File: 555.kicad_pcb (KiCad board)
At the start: 2 copper layers, 120 x 35 mm, 62 parts, among them J2 Screw_Terminal_01x02, P1 USB_C_Plug, SW1 SW_Push, SW2 SW_Push, SW3 SW_Push, SW4 SW_Push, SW5 SW_Push, SW6 SW_Push, SW7 SW_Push, SW8 SW_Push, U1 NE555P

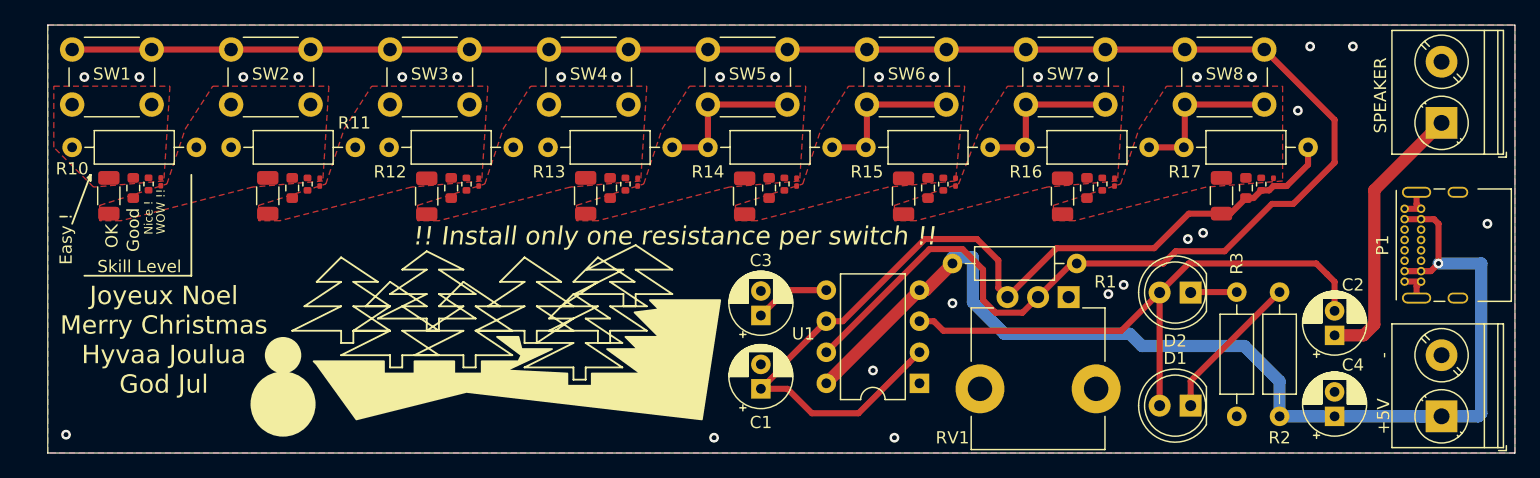
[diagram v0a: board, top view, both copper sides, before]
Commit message: Simpler, remove the 10k resistor, move the potentiometer to full to play
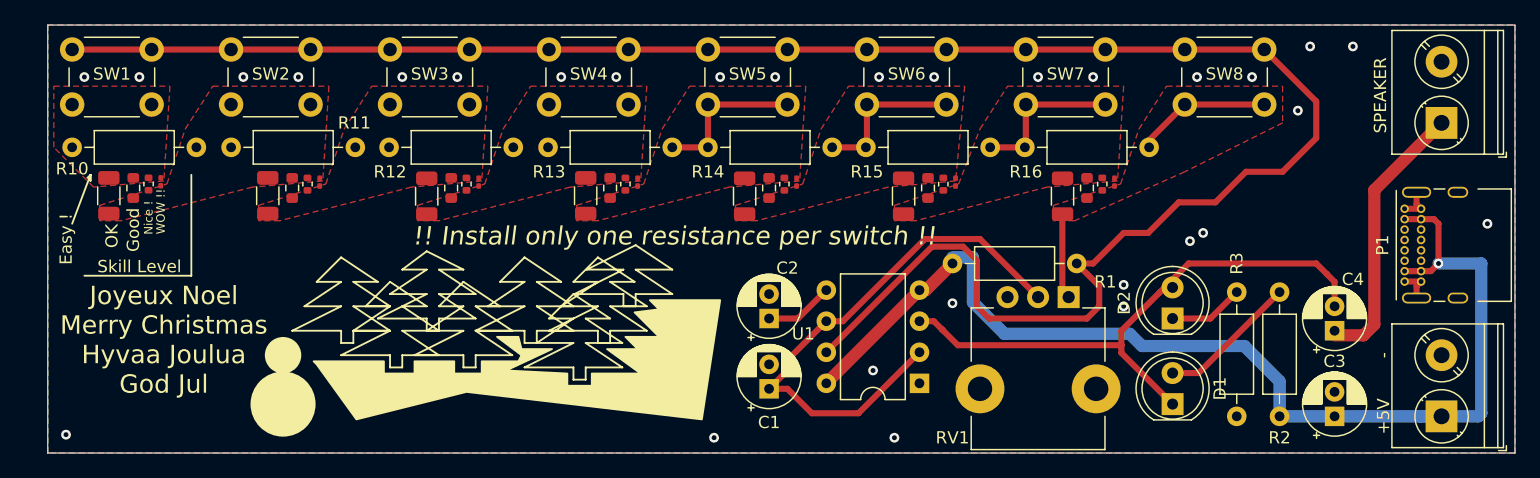
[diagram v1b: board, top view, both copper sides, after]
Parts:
- removed R17: 10k, Resistor_THT:R_Axial_DIN0207_L6.3mm_D2.5mm_P10.16mm_Horizontal
- removed R27: 10k, Resistor_SMD:R_1206_3216Metric
- removed R37: 10k, Resistor_SMD:R_0603_1608Metric
- removed R47: 10k, Resistor_SMD:R_0402_1005Metric
- removed R57: 10k, Resistor_SMD:R_0201_0603Metric
- C2: value 4.7uF -> 10uF
- C4: value 10uF -> 4.7uF
- moved C3 47.6 mm to (136.2, 89.0)
- moved C2 46.3 mm to (90.0, 81.0)
- moved C4 7.00 mm to (136.2, 82.0)
- moved D2 2.59 mm to (123.0, 81.0), turned to 90 degrees
- moved D1 1.49 mm to (123.0, 88.0), turned to 90 degrees
- moved C1 0.67 mm to (90.0, 86.8)
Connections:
- C1 pad 1: Net-(C1-Pad1) -> Net-(RV1-Pad2)
- C2 pad 1: Net-(LS1-Pad1) -> Net-(U1-Pad5)
- C2 pad 2: Net-(D1-Pad2) -> GND
- C3 pad 1: Net-(U1-Pad5) -> +5V
- C4 pad 1: +5V -> Net-(C4-Pad1)
- C4 pad 2: GND -> Net-(C4-Pad2)
- D1 pad 1: Net-(D1-Pad1) -> Net-(C4-Pad2)
- D1 pad 2: Net-(D1-Pad2) -> Net-(R2-Pad2)
- D2 pad 2: Net-(D1-Pad2) -> Net-(C4-Pad2)
- LS1 pad 1: Net-(LS1-Pad1) -> Net-(C4-Pad1)
- R1 pad 2: Net-(R1-Pad2) -> Net-(SW1-Pad2)
- R2 pad 2: Net-(D1-Pad1) -> Net-(R2-Pad2)
- RV1 pad 1: unconnected-(RV1-Pad1) -> Net-(R16-Pad2)
- RV1 pad 2: Net-(R1-Pad2) -> Net-(RV1-Pad2)
- RV1 pad 3: Net-(C1-Pad1) -> unconnected-(RV1-Pad3)
- SW1 pad 2: Net-(R1-Pad2) -> Net-(SW1-Pad2)
- SW2 pad 2: Net-(R1-Pad2) -> Net-(SW1-Pad2)
- SW3 pad 2: Net-(R1-Pad2) -> Net-(SW1-Pad2)
- SW4 pad 2: Net-(R1-Pad2) -> Net-(SW1-Pad2)
- SW5 pad 2: Net-(R1-Pad2) -> Net-(SW1-Pad2)
- SW6 pad 2: Net-(R1-Pad2) -> Net-(SW1-Pad2)
- SW7 pad 2: Net-(R1-Pad2) -> Net-(SW1-Pad2)
- SW8 pad 2: Net-(R1-Pad2) -> Net-(SW1-Pad2)
- U1 pad 2: Net-(C1-Pad1) -> Net-(RV1-Pad2)
- U1 pad 3: Net-(D1-Pad2) -> Net-(C4-Pad2)
- U1 pad 6: Net-(C1-Pad1) -> Net-(RV1-Pad2)
- U1 pad 7: Net-(R1-Pad2) -> Net-(SW1-Pad2)
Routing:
- net Net-(SW1-Pad2): track 0.00 -> 166.0 mm
- net Net-(R1-Pad2): track 162.9 -> 0.00 mm
- net Net-(C1-Pad1): track 75.0 -> 0.00 mm
- net Net-(D1-Pad2): track 48.8 -> 0.00 mm
- net Net-(C4-Pad2): track 0.00 -> 47.9 mm
- net Net-(RV1-Pad2): track 0.00 -> 44.7 mm
- net Net-(LS1-Pad1): track 22.4 -> 0.00 mm
- net Net-(C4-Pad1): track 0.00 -> 22.4 mm
- net Net-(D1-Pad1): track 12.3 -> 0.00 mm
- net Net-(R2-Pad2): track 0.00 -> 11.5 mm
- net Net-(R16-Pad2): track 12.9 -> 18.2 mm
- net Net-(D2-Pad1): track 3.78 -> 6.14 mm
- net Net-(U1-Pad5): track 6.21 -> 5.64 mm

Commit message: PCB updated
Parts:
- C4: value 4.7uF -> 10uF
- moved C4 1.65 mm to (136.2, 80.3), turned to -90 degrees
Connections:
- C4 pad 1: Net-(C4-Pad1) -> Net-(D1-Pad1)
- C4 pad 2: Net-(C4-Pad2) -> Net-(LS1-Pad1)
- D1 pad 1: Net-(C4-Pad2) -> Net-(D1-Pad1)
- D2 pad 2: Net-(C4-Pad2) -> Net-(D1-Pad1)
- LS1 pad 1: Net-(C4-Pad1) -> Net-(LS1-Pad1)
- U1 pad 3: Net-(C4-Pad2) -> Net-(D1-Pad1)
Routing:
- net Net-(C4-Pad2): track 47.9 -> 0.00 mm
- net Net-(D1-Pad1): track 0.00 -> 47.8 mm
- net Net-(LS1-Pad1): track 0.00 -> 22.4 mm
- net Net-(C4-Pad1): track 22.4 -> 0.00 mm

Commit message: Prettier sch
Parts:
- P1: value USB_C_Plug -> USB_C_Plug_USB2.0
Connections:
- P1 pad A8: unconnected-(P1-PadA8) -> (no net)
- P1 pad B8: unconnected-(P1-PadB8) -> (no net)
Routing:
- net GND: vias 29 -> 51

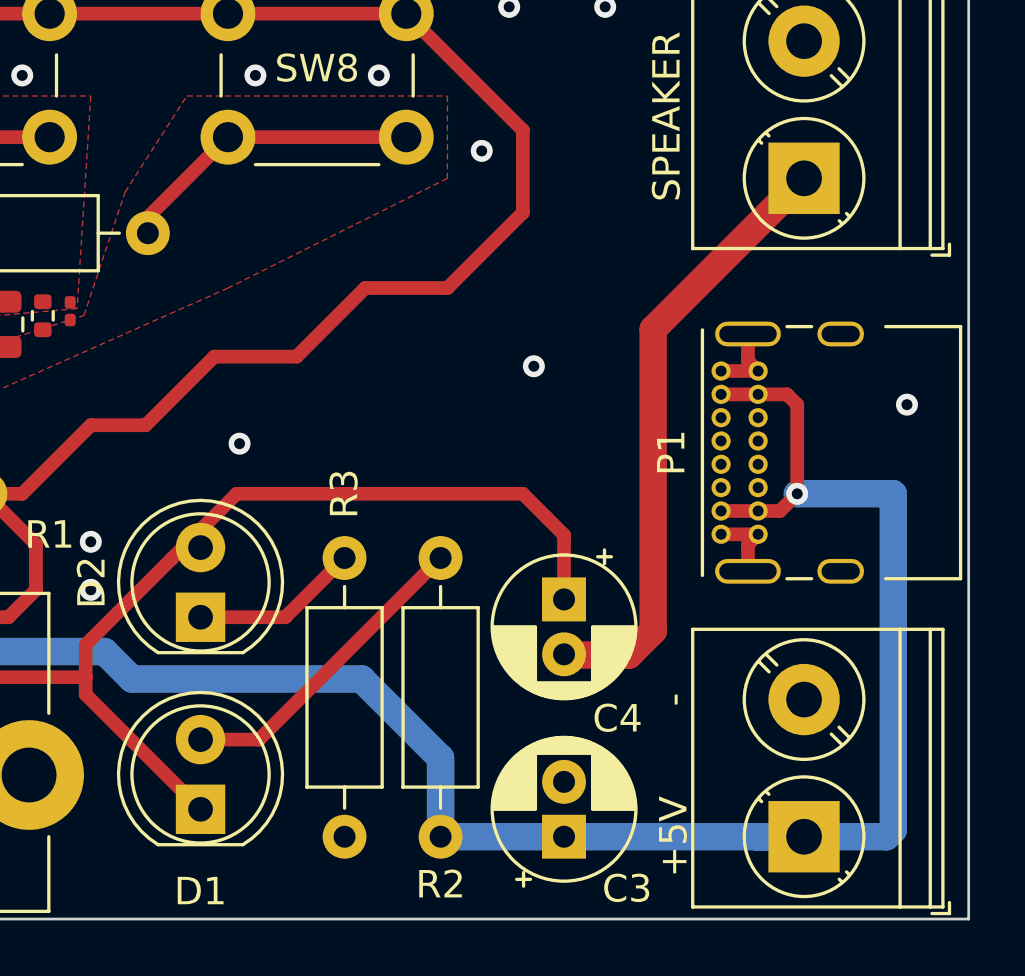
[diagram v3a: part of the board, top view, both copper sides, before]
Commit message: USB-C resistor CC
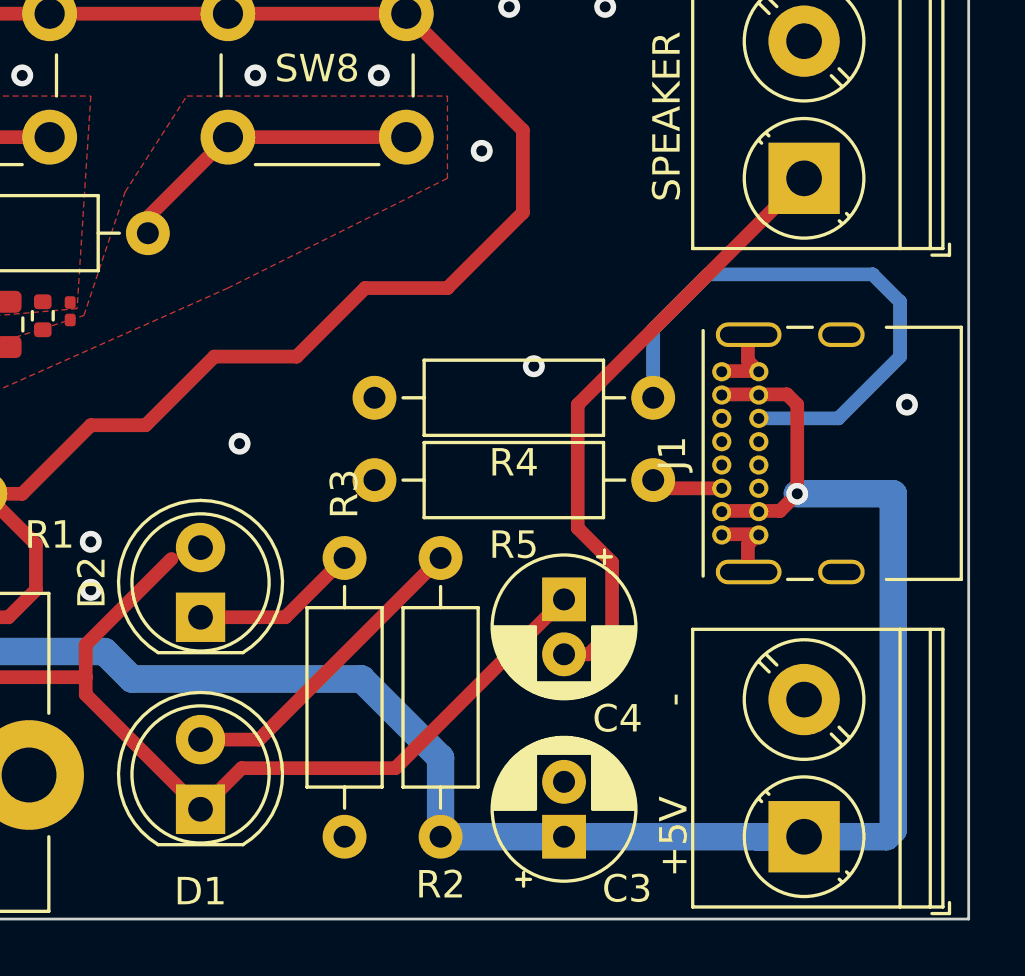
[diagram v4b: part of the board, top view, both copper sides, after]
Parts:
- removed P1: USB_C_Plug_USB2.0, Connector_USB:USB_C_Receptacle_GCT_USB4085
- added J1: USB_C_Receptacle_USB2.0, Connector_USB:USB_C_Receptacle_GCT_USB4085, F.Cu at (142.0, 78.0)
- added R4: 5.1k, Resistor_THT:R_Axial_DIN0207_L6.3mm_D2.5mm_P10.16mm_Horizontal, F.Cu at (139.5, 73.0)
- added R5: 5.1k, Resistor_THT:R_Axial_DIN0207_L6.3mm_D2.5mm_P10.16mm_Horizontal, F.Cu at (139.5, 76.0)
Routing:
- net Net-(J1-PadB5): track 0.00 -> 20.8 mm
- net Net-(J1-PadA5): track 0.00 -> 2.62 mm
- net Net-(C4-Pad1): track 47.8 -> 45.9 mm

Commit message: Art contribution AML
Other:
- board text added: "AML"
